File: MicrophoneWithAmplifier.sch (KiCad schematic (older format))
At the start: 8 parts, among them U1 TL082CP

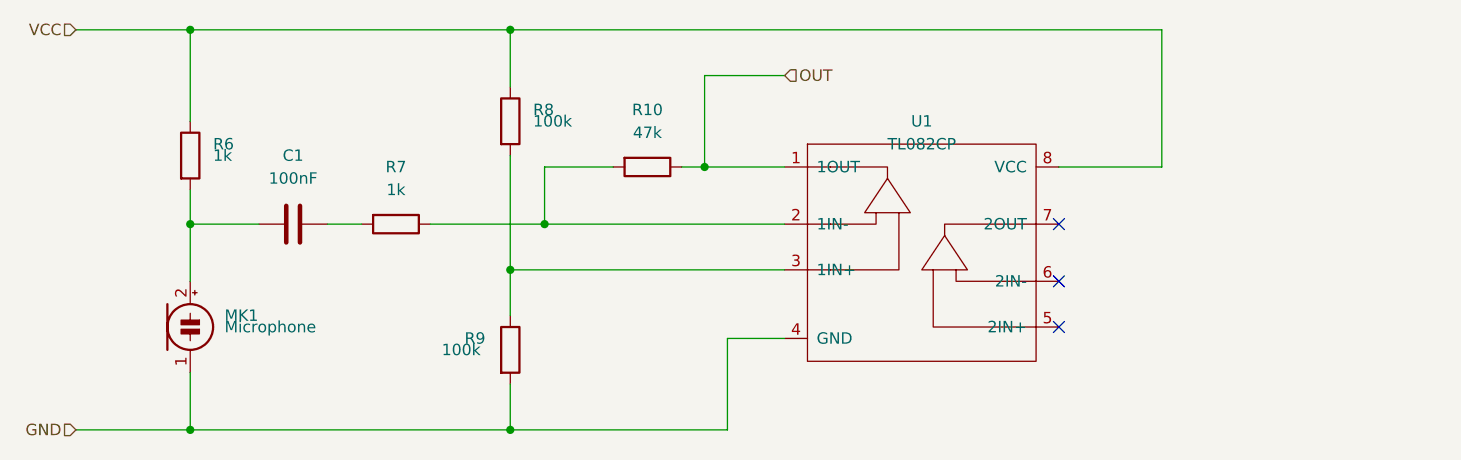
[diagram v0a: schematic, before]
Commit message: add a comparator for setting up an interrupt
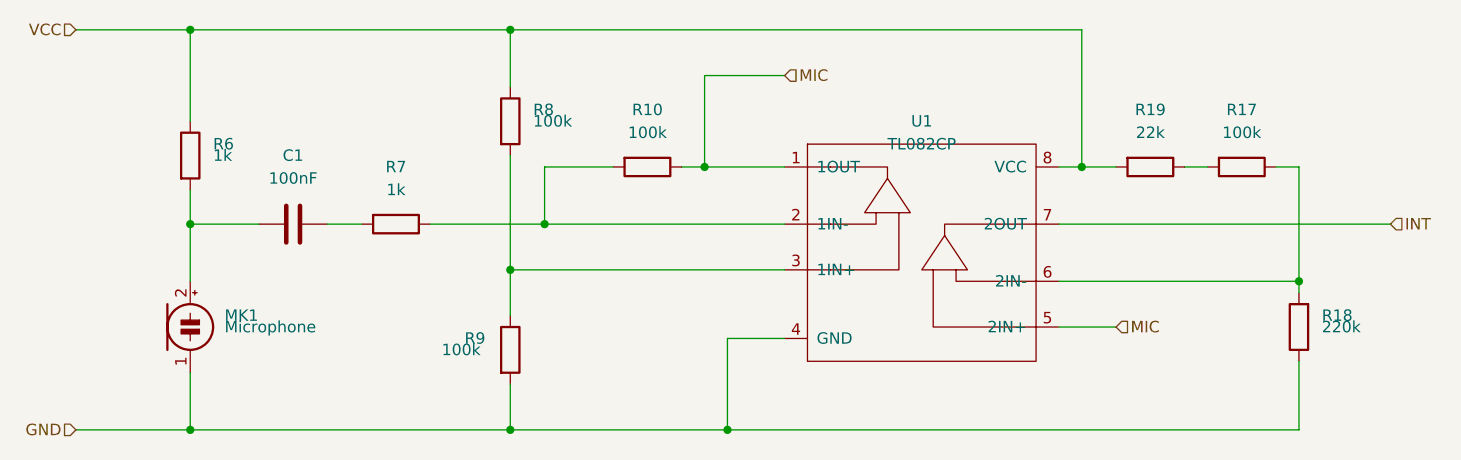
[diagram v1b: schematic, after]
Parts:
- added R17: 100k, symbol Device:R
- added R18: 220k, symbol Device:R
- added R19: 22k, symbol Device:R
- R10: value 47k -> 100k
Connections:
- net OUT is gone; now on net MIC: R10.1, U1.1 (1OUT)
- net GND: now also R18.1
- net VCC: now also R19.2
- net MIC: now reaches U1.5 (2IN+)
- net at U1.6 (2IN-): now also R17.1, R18.2
- net INT: now reaches U1.7 (2OUT)
- new net: R17.2, R19.1
- no-connect marks 3 -> 0
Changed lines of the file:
@@
 Sheet 2 4
 Title "Microphone with amplifier"
-Date "2020-04-10"
+Date "2020-04-11"
 Rev "1"
 Comp "Džejky"
@@
 P 6050 3750
 F 0 "R10" V 5800 3750 50  0000 C CNN
-F 1 "47k" V 5900 3750 50  0000 C CNN
+F 1 "100k" V 5900 3750 50  0000 C CNN
 F 2 "Resistor_THT:R_Axial_DIN0411_L9.9mm_D3.6mm_P15.24mm_Horizontal" V 5980 3750 50  0001 C CNN
 F 3 "~" H 6050 3750 50  0001 C CNN
@@
 $EndComp
 Text HLabel 6650 3350 2    50   Input ~ 0
-OUT
+MIC
 $Comp
 L Device:Microphone_Condenser MK1
@@
 Wire Wire Line
 	5600 4000 6650 4000
-NoConn ~ 7850 4000
-NoConn ~ 7850 4250
-NoConn ~ 7850 4450
-Wire Wire Line
-	7850 3750 8300 3750
-Wire Wire Line
-	8300 3750 8300 3150
-Wire Wire Line
-	5450 3150 8300 3150
+Wire Wire Line
+	7850 3750 7950 3750
+Wire Wire Line
+	7950 3750 7950 3150
+Wire Wire Line
+	5450 3150 7950 3150
 Wire Wire Line
 	6200 3750 6300 3750
@@
 Wire Wire Line
 	6300 3750 6650 3750
+Wire Wire Line
+	7850 4000 9300 4000
+Text HLabel 9300 4000 2    50   Input ~ 0
+INT
+Text HLabel 8100 4450 2    50   Input ~ 0
+MIC
+Wire Wire Line
+	8100 4450 7850 4450
+$Comp
+L Device:R R17
+U 1 1 5E9831A3
+P 8650 3750
+F 0 "R17" V 8400 3750 50  0000 C CNN
+F 1 "100k" V 8500 3750 50  0000 C CNN
+F 2 "" V 8580 3750 50  0001 C CNN
+F 3 "~" H 8650 3750 50  0001 C CNN
+	1    8650 3750
+	0    1    1    0
+$EndComp
+$Comp
+L Device:R R18
+U 1 1 5E983950
+P 8900 4450
+F 0 "R18" H 8800 4400 50  0000 R CNN
+F 1 "220k" H 8800 4450 50  0000 R CNN
+F 2 "" V 8830 4450 50  0001 C CNN
+F 3 "~" H 8900 4450 50  0001 C CNN
+	1    8900 4450
+	-1   0    0    1
+$EndComp
+Wire Wire Line
+	7850 4250 8900 4250
+Wire Wire Line
+	8900 4250 8900 4300
+Wire Wire Line
+	8900 4250 8900 3750
+Connection ~ 8900 4250
+Wire Wire Line
+	8900 4600 8900 4900
+Wire Wire Line
+	8900 4900 6400 4900
+Connection ~ 6400 4900
+$Comp
+L Device:R R19
+U 1 1 5E98D539
+P 8250 3750
+F 0 "R19" V 8000 3750 50  0000 C CNN
+F 1 "22k" V 8100 3750 50  0000 C CNN
+F 2 "" V 8180 3750 50  0001 C CNN
+F 3 "~" H 8250 3750 50  0001 C CNN
+	1    8250 3750
+	0    1    1    0
+$EndComp
+Wire Wire Line
+	8800 3750 8900 3750
+Wire Wire Line
+	8500 3750 8400 3750
+Wire Wire Line
+	8100 3750 7950 3750
+Connection ~ 7950 3750
 $EndSCHEMATC

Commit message: add the RTC module and base prototype pcb layout
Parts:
- C1: footprint (none) -> Capacitor_THT:C_Disc_D3.4mm_W2.1mm_P2.50mm
- MK1: footprint Capacitor_THT:CP_Radial_Tantal_D6.0mm_P2.50mm -> Capacitor_THT:CP_Radial_Tantal_D9.0mm_P2.50mm
- R10, R6, R7, R8, R9: footprint Resistor_THT:R_Axial_DIN0411_L9.9mm_D3.6mm_P15.24mm_Horizontal -> Resistor_THT:R_Axial_DIN0207_L6.3mm_D2.5mm_P7.62mm_Horizontal
- R17, R18, R19: footprint (none) -> Resistor_THT:R_Axial_DIN0207_L6.3mm_D2.5mm_P7.62mm_Horizontal
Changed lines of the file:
@@
 F 0 "R8" H 5550 3600 50  0000 L CNN
 F 1 "100k" H 5550 3550 50  0000 L CNN
-F 2 "Resistor_THT:R_Axial_DIN0411_L9.9mm_D3.6mm_P15.24mm_Horizontal" V 5380 3550 50  0001 C CNN
+F 2 "Resistor_THT:R_Axial_DIN0207_L6.3mm_D2.5mm_P7.62mm_Horizontal" V 5380 3550 50  0001 C CNN
 F 3 "~" H 5450 3550 50  0001 C CNN
 	1    5450 3550
@@
 F 0 "R9" H 5250 4600 50  0000 L CNN
 F 1 "100k" H 5150 4550 50  0000 L CNN
-F 2 "Resistor_THT:R_Axial_DIN0411_L9.9mm_D3.6mm_P15.24mm_Horizontal" V 5380 4550 50  0001 C CNN
+F 2 "Resistor_THT:R_Axial_DIN0207_L6.3mm_D2.5mm_P7.62mm_Horizontal" V 5380 4550 50  0001 C CNN
 F 3 "~" H 5450 4550 50  0001 C CNN
 	1    5450 4550
@@
 F 0 "R7" V 4700 4000 50  0000 C CNN
 F 1 "1k" V 4800 4000 50  0000 C CNN
-F 2 "Resistor_THT:R_Axial_DIN0411_L9.9mm_D3.6mm_P15.24mm_Horizontal" V 4880 4000 50  0001 C CNN
+F 2 "Resistor_THT:R_Axial_DIN0207_L6.3mm_D2.5mm_P7.62mm_Horizontal" V 4880 4000 50  0001 C CNN
 F 3 "~" H 4950 4000 50  0001 C CNN
 	1    4950 4000
@@
 F 0 "C1" V 4200 4000 50  0000 C CNN
 F 1 "100nF" V 4300 4000 50  0000 C CNN
-F 2 "" H 4538 3850 50  0001 C CNN
+F 2 "Capacitor_THT:C_Disc_D3.4mm_W2.1mm_P2.50mm" H 4538 3850 50  0001 C CNN
 F 3 "~" H 4500 4000 50  0001 C CNN
 	1    4500 4000
@@
 F 0 "R6" H 4150 3750 50  0000 L CNN
 F 1 "1k" H 4150 3700 50  0000 L CNN
-F 2 "Resistor_THT:R_Axial_DIN0411_L9.9mm_D3.6mm_P15.24mm_Horizontal" V 3980 3700 50  0001 C CNN
+F 2 "Resistor_THT:R_Axial_DIN0207_L6.3mm_D2.5mm_P7.62mm_Horizontal" V 3980 3700 50  0001 C CNN
 F 3 "~" H 4050 3700 50  0001 C CNN
 	1    4050 3700
@@
 F 0 "R10" V 5800 3750 50  0000 C CNN
 F 1 "100k" V 5900 3750 50  0000 C CNN
-F 2 "Resistor_THT:R_Axial_DIN0411_L9.9mm_D3.6mm_P15.24mm_Horizontal" V 5980 3750 50  0001 C CNN
+F 2 "Resistor_THT:R_Axial_DIN0207_L6.3mm_D2.5mm_P7.62mm_Horizontal" V 5980 3750 50  0001 C CNN
 F 3 "~" H 6050 3750 50  0001 C CNN
 	1    6050 3750
@@
 F 0 "MK1" H 4200 4500 50  0000 L CNN
 F 1 "Microphone" H 4200 4450 50  0000 L CNN
-F 2 "Capacitor_THT:CP_Radial_Tantal_D6.0mm_P2.50mm" V 4050 4550 50  0001 C CNN
+F 2 "Capacitor_THT:CP_Radial_Tantal_D9.0mm_P2.50mm" V 4050 4550 50  0001 C CNN
 F 3 "~" V 4050 4550 50  0001 C CNN
 	1    4050 4450
@@
 F 0 "R17" V 8400 3750 50  0000 C CNN
 F 1 "100k" V 8500 3750 50  0000 C CNN
-F 2 "" V 8580 3750 50  0001 C CNN
+F 2 "Resistor_THT:R_Axial_DIN0207_L6.3mm_D2.5mm_P7.62mm_Horizontal" V 8580 3750 50  0001 C CNN
 F 3 "~" H 8650 3750 50  0001 C CNN
 	1    8650 3750
@@
 F 0 "R18" H 8800 4400 50  0000 R CNN
 F 1 "220k" H 8800 4450 50  0000 R CNN
-F 2 "" V 8830 4450 50  0001 C CNN
+F 2 "Resistor_THT:R_Axial_DIN0207_L6.3mm_D2.5mm_P7.62mm_Horizontal" V 8830 4450 50  0001 C CNN
 F 3 "~" H 8900 4450 50  0001 C CNN
 	1    8900 4450
@@
 F 0 "R19" V 8000 3750 50  0000 C CNN
 F 1 "22k" V 8100 3750 50  0000 C CNN
-F 2 "" V 8180 3750 50  0001 C CNN
+F 2 "Resistor_THT:R_Axial_DIN0207_L6.3mm_D2.5mm_P7.62mm_Horizontal" V 8180 3750 50  0001 C CNN
 F 3 "~" H 8250 3750 50  0001 C CNN
 	1    8250 3750

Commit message: make the pcb design
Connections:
- net MIC+: now reaches C1.2, MK1.2 (+), R6.2
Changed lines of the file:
@@
 	8100 3750 7950 3750
 Connection ~ 7950 3750
+Text Label 4050 4000 2    50   ~ 0
+MIC+
 $EndSCHEMATC
